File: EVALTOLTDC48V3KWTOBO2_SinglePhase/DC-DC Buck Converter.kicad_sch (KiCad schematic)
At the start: 39 parts, among them J3 EXT/ITN 12V, J4 +12V_EXT, J5 +5V_EXT, Q9 FMMT723/SOT, U1 ILD8150XUMA1

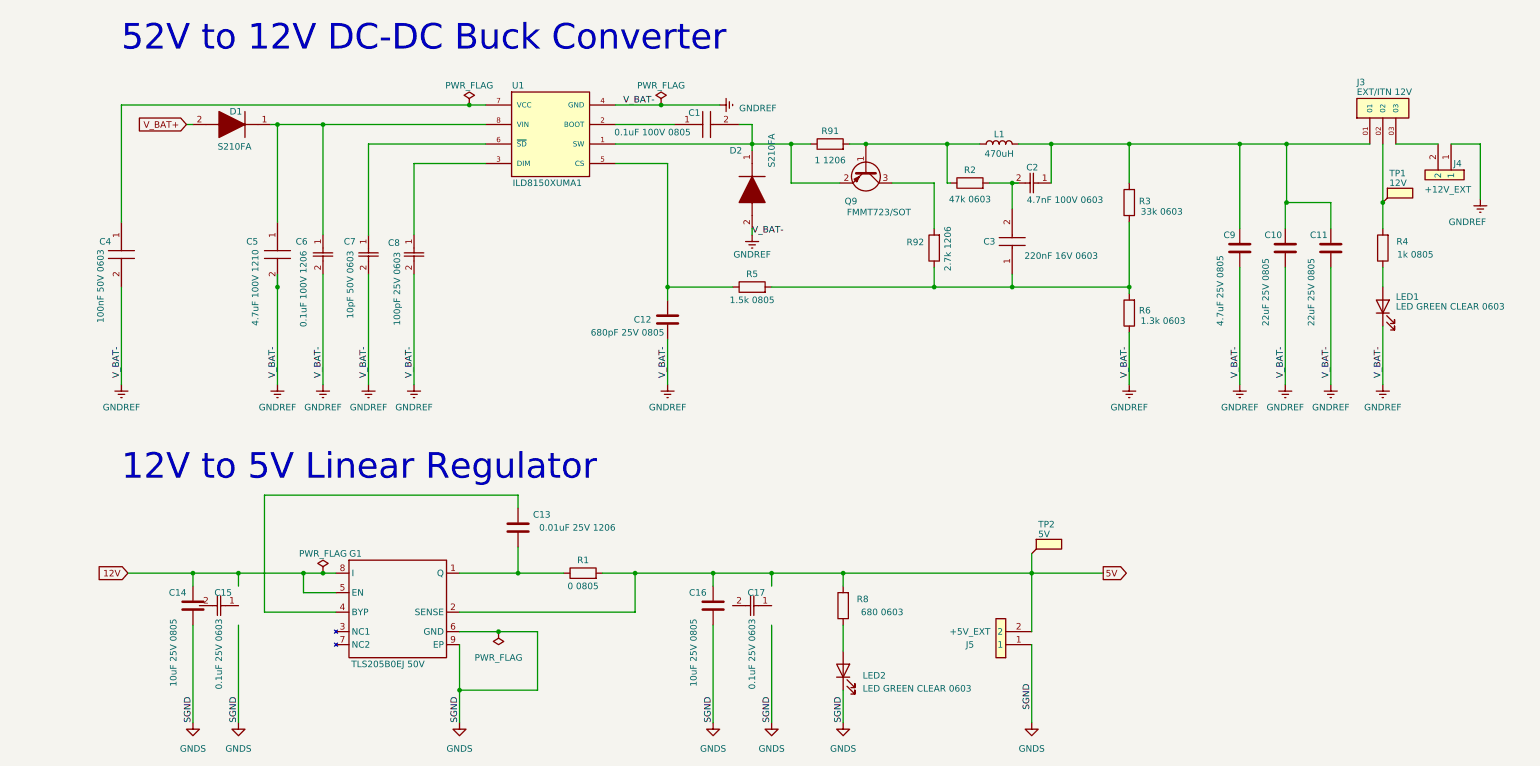
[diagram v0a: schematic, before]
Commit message: Change 1
Changed DC-DC Buck Converter and U Phase
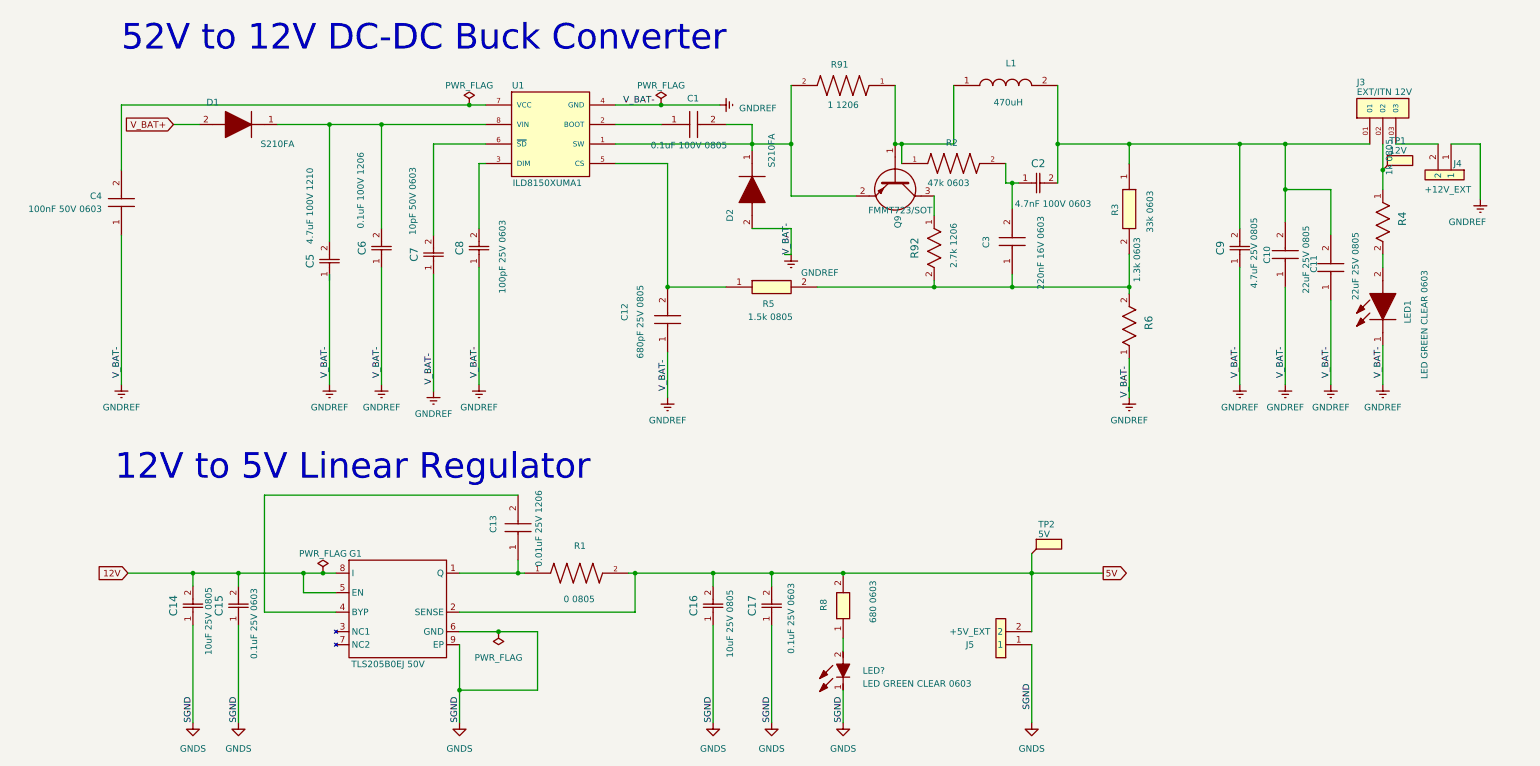
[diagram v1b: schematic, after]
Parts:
- C1: footprint just-footprints:C0805 -> C0805
- C10, C11: footprint (none) -> CAPC2012X145N; symbol Device:C -> C2012X7S1A226M125AC:C2012X7S1A226M125AC; Height (none) -> 1.45; Manufacturer_Name (none) -> TDK; Manufacturer_Part_Number (none) -> C2012X7S1A226M125AC
- C12: footprint (none) -> C1206C103J3RACAUTO:C1206; symbol Device:C -> C1206C103J3RACAUTO:C1206C103J3RACAUTO; Manufacturer_Name (none) -> KEMET; Manufacturer_Part_Number (none) -> C1206C103J3RACAUTO; Mouser Part Number (none) -> 80-C1206C103J3RAUTO; Mouser Price/Stock (none) -> https://www.mouser.co.uk/ProductDetail/KEMET/C1206C103J3RAC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
- C13: footprint (none) -> C1206; symbol Device:C -> C1206C103J3RACAUTO:C1206C103J3RACAUTO; Manufacturer_Name (none) -> KEMET; Manufacturer_Part_Number (none) -> C1206C103J3RACAUTO; Mouser Part Number (none) -> 80-C1206C103J3RAUTO; Mouser Price/Stock (none) -> https://www.mouser.co.uk/ProductDetail/KEMET/C1206C103J3RAC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
- C14, C16: footprint (none) -> CAPC220145_145N_KEM; symbol Device:C -> C0805C106M3PACTU:C0805C106M3PACTU
- C15, C17: footprint just-footprints:CAPC17795_95N_KEM -> CAPC17795_95N_KEM; symbol C0603X104M3RAUTO:C0603X104M3RACTU -> C0603X104M3RACTU:C0603X104M3RACTU
- C2: footprint just-footprints:CAPC17795_95N_KEM -> CAPC17795_95N_KEM
- C3: footprint just-footprints:C0603 -> C0603
- C4: footprint just-footprints:CAPC1608X95N -> CAPC1608X95N
- C5: footprint just-footprints:CAPC3225X280N -> CAP_CNC6_TDK; symbol CNA6P1X7R2A475K250AE:CNA6P1X7R2A475K250AE -> CNC6P1X7R2A475K250AE:CNC6P1X7R2A475K250AE; Height 2.8 -> (none); Manufacturer_Name TDK -> (none); Manufacturer_Part_Number CNA6P1X7R2A475K250AE -> (none); Mouser Part Number 810-CNA6P1X7R2A475K2 -> (none); Mouser Price/Stock https://www.mouser.co.uk/ProductDetail/TDK/CNA6P1X7R2A475K2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 -> (none)
- C6: footprint just-footprints:CAP_C1206F-RAC-ER_KEM -> CAP_C1206F-RAC-ER_KEM
- C7: footprint just-footprints:CAPC17595_87N_KEM -> CAPC17595_87N_KEM
- C8: footprint just-footprints:CAPC10555_55N_KEM -> CAPC17595_87N_KEM; symbol C0603C101K3RACAUTO:C0402C101K3RACTU -> C0603C101K3RACAUTO:C0603C101K3RACAUTO
- C9: footprint (none) -> CAPC220145_88N_KEM; symbol Device:C -> C0805X475K3RAC7800:C0805C681J5RACTU
- D1, D2: footprint just-footprints:SODFL3618X143N -> SODFL3618X143N
- G1: footprint (none) -> TLS205B0EJV50XUMA1:SOIC127P600X170-9N
- J4, J5: footprint just-footprints:1725656 -> 1725656
- L1: footprint (none) -> WE-PD_1260/1245/1280/121054; symbol Device:L -> 7447709471:7447709471; Manufacturer_Name (none) -> Wurth Elektronik; Manufacturer_Part_Number (none) -> 7447709471; Mouser Part Number (none) -> 710-7447709471; Mouser Price/Stock (none) -> https://www.mouser.co.uk/ProductDetail/Wurth-Elektronik/744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
- LED1: footprint (none) -> LEDC1608X80N; symbol Device:LED -> LTST-C190KGKT:LTST-C190KGKT; Arrow Part Number (none) -> LTST-C190KGKT; Arrow Price/Stock (none) -> https://www.arrow.com/en/products/ltst-c190kgkt/lite-on-tec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; Height (none) -> 0.8; Manufacturer_Name (none) -> Lite-On; Manufacturer_Part_Number (none) -> LTST-C190KGKT; Mouser Part Number (none) -> 859-LTST-C190KGKT; Mouser Price/Stock (none) -> https://www.mouser.co.uk/ProductDetail/Lite-On/LTST-C190KGK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
- LED?: renamed from LED2; footprint (none) -> LEDC1608X80N; symbol Device:LED -> LTST-C190KGKT:LTST-C190KGKT; Arrow Part Number (none) -> LTST-C190KGKT; Arrow Price/Stock (none) -> https://www.arrow.com/en/products/ltst-c190kgkt/lite-on-tec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; Height (none) -> 0.8; Manufacturer_Name (none) -> Lite-On; Manufacturer_Part_Number (none) -> LTST-C190KGKT; Mouser Part Number (none) -> 859-LTST-C190KGKT; Mouser Price/Stock (none) -> https://www.mouser.co.uk/ProductDetail/Lite-On/LTST-C190KGK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
- Q9: footprint Package_TO_SOT_SMD:SOT-23 -> SOT96P240X110-3N; symbol Transistor_BJT:BC858 -> FMMT723QTA:FMMT723QTA; Height (none) -> 1.1; Manufacturer_Name (none) -> Diodes Incorporated; Manufacturer_Part_Number (none) -> FMMT723QTA; Mouser Part Number (none) -> 621-FMMT723QTA; Mouser Price/Stock (none) -> https://www.mouser.co.uk/ProductDetail/Diodes-Incorporated/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
- R1: footprint (none) -> RCS08050000Z0EA:RESC2012X50N; symbol Device:R -> RCS08050000Z0EA:RCS08050000Z0EA
- R2: footprint (none) -> RCS060347K0FKEA:RESC1508X50N; symbol Device:R -> RCS060347K0FKEA:RCS060347K0FKEA
- R3: footprint (none) -> RESC1608X50N; symbol Device:R -> RCS060333K0FKEA:RCS060333K0FKEA; Height (none) -> 0.5; Manufacturer_Name (none) -> Vishay; Manufacturer_Part_Number (none) -> RCS060333K0FKEA; Mouser Part Number (none) -> 71-RCS060333K0FKEA; Mouser Price/Stock (none) -> https://www.mouser.co.uk/ProductDetail/Vishay-Dale/RCS06033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
- R4: footprint (none) -> RES_RCA0805_VIS; symbol Device:R -> RCA08051K00FKEAHP:RCA08051K00FKEAHP
- R5: footprint (none) -> RESC1608X50N; symbol Device:R -> CRCW06031R20JNEAIF:CRCW06031R20JNEAIF; Height (none) -> 0.5; Manufacturer_Name (none) -> Vishay; Manufacturer_Part_Number (none) -> CRCW06031R20JNEAIF
- R6: footprint (none) -> RC0603N_VIS; symbol Device:R -> CRCW06031K10FKTA:CRCW06031K10FKTA
- R8: footprint (none) -> RCS0603_E3; symbol Device:R -> RCS0603680RFKEA:RCS0603680RFKEA; Manufacturer_Name (none) -> Vishay; Manufacturer_Part_Number (none) -> RCS0603680RFKEA; Mouser Part Number (none) -> 71-RCS0603680RFKEA; Mouser Price/Stock (none) -> https://www.mouser.co.uk/ProductDetail/Vishay-Dale/RCS06036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
- R91: footprint (none) -> CRCW12061R00FNEB:RESC3116X60N; symbol Device:R -> CRCW12061R00FNEB:CRCW12061R00FNEB
- R92: footprint (none) -> RES_V1206_VIS; symbol Device:R -> CRCW12062K70JNEAHP:CRCW12062K70JNEAHP
- U1: footprint ILD8150XUMA1:SOIC127P600X175-8N -> ILD8150:SOIC127P600X175-8N
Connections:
- net 12V: now also C15.2
- net 5V: now also C17.2
- net GNDREF: now also C10.1, C11.1, C4.1, C6.1, C7.1, C8.1, C9.1; no longer C10.2, C11.2, C4.2, C5.2, C6.2, C7.2, C8.2, C9.2
- net GNDS: now also C15.1, C17.1
- net at U1.3 (DIM): now also C8.2; no longer C8.1
- net at C3.2, R2.2: now also C2.1; no longer C2.2
- net at C1.2, D2.1 (K), Q9.2 (E)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: now also R91.2; no longer R91.1
- net at U1.6 (~{SD}): now also C7.2; no longer C7.1
- net at U1.7 (VCC): now also C4.2; no longer C4.1
- net at D1.1 (K), U1.8 (VIN): now also C5.2, C6.2; no longer C5.1, C6.1
- net at C3.1, R5.2, R6.2: now also R3.2, R92.2; no longer R3.1, R92.1
- net at R4.1: now also J3.02, TP1.1; no longer LED1.2 (A)
- net at Q9.3 (C): now also R92.1; no longer R92.2
- net at L1.1, Q9.1 (B), R2.1: now also R91.1; no longer R91.2
- new net: C10.2, C11.2, C2.2, C9.2, J3.01, L1.2, R3.1
- new net: LED1.2 (A), R4.2
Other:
- moved on the sheet: C1, C15, C17, C2, C4, C5, C6, C7, C8, D1, TP1

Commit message: Change 3
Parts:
- gave numbers to parts that had none: 1
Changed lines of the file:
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@@
 	(text "12V to 5V Linear Regulator"
 		(exclude_from_sim no)
-		(at 16.51 110.49 0)
+		(at 14.478 106.426 0)
 		(effects
 			(font
@@
 		(on_board yes)
 		(dnp no)
-		(fields_autoplaced yes)
 		(property "Reference" "C4"
-			(at 13.97 54.6099 90)
+			(at 24.384 54.61 90)
 			(effects
 				(font
@@
 		)
 		(property "Value" "100nF 50V 0603"
-			(at 13.97 57.1499 90)
+			(at 37.338 57.912 90)
 			(effects
 				(font
@@
 		(dnp no)
 		(fields_autoplaced yes)
-		(property "Reference" "LED?"
+		(property "Reference" "LED2"
 			(at 162.56 147.3199 90)
 			(effects
@@
 			(project "EVAL_TOLT_DC48V_3KW"
 				(path "/ab32ac57-1c18-4307-8f91-d2778314d165/9ee2cd02-96d7-461b-b7fb-170453b1d10b"
-					(reference "LED?")
+					(reference "LED2")
 					(unit 1)
 				)
@@
 		(dnp no)
 		(property "Reference" "D1"
-			(at 36.83 35.56 0)
+			(at 36.576 43.942 0)
 			(effects
 				(font

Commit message: Change 3
Added More Symbols and Footprints
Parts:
- C1: footprint C0805 -> just-footprints:C0805
- C10, C11: footprint CAPC2012X145N -> just-footprints:CAPC2012X145N
- C13: footprint C1206 -> just-footprints:C1206
- C14, C16: footprint CAPC220145_145N_KEM -> just-footprints:CAPC220145_145N_KEM
- C15, C17, C2: footprint CAPC17795_95N_KEM -> just-footprints:CAPC17795_95N_KEM
- C3: footprint C0603 -> just-footprints:C0603
- C4: footprint CAPC1608X95N -> just-footprints:CAPC1608X95N
- C5: footprint CAP_CNC6_TDK -> just-footprints:CAP_CNC6_TDK
- C6: footprint CAP_C1206F-RAC-ER_KEM -> just-footprints:CAP_C1206F-RAC-ER_KEM
- C7, C8: footprint CAPC17595_87N_KEM -> just-footprints:CAPC17595_87N_KEM
- C9: footprint CAPC220145_88N_KEM -> just-footprints:CAPC220145_88N_KEM
- D1, D2: footprint SODFL3618X143N -> just-footprints:SODFL3618X143N
- J4, J5: footprint 1725656 -> just-footprints:1725656
- LED1, LED2: footprint LEDC1608X80N -> just-footprints:LEDC1608X80N
- Q9: footprint SOT96P240X110-3N -> just-footprints:SOT96P240X110-3N
- R3, R5: footprint RESC1608X50N -> just-footprints:RESC1608X50N
- R4: footprint RES_RCA0805_VIS -> just-footprints:RES_RCA0805_VIS
- R6: footprint RC0603N_VIS -> just-footprints:RC0603N_VIS
- R8: footprint RCS0603_E3 -> just-footprints:RCS0603_E3
- R92: footprint RES_V1206_VIS -> just-footprints:RES_V1206_VIS
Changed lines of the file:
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@@
 			)
 		)
-		(property "Footprint" "CAPC2012X145N"
+		(property "Footprint" "just-footprints:CAPC2012X145N"
 			(at 350.19 66.04 0)
 			(effects
@@
 			)
 		)
-		(property "Footprint" "CAPC220145_145N_KEM"
+		(property "Footprint" "just-footprints:CAPC220145_145N_KEM"
 			(at 133.35 138.43 0)
 			(effects
@@
 			)
 		)
-		(property "Footprint" "CAPC220145_88N_KEM"
+		(property "Footprint" "just-footprints:CAPC220145_88N_KEM"
 			(at 236.22 68.58 0)
 			(effects
@@
 			)
 		)
-		(property "Footprint" "CAPC17595_87N_KEM"
+		(property "Footprint" "just-footprints:CAPC17595_87N_KEM"
 			(at 87.63 68.58 0)
 			(effects
@@
 			)
 		)
-		(property "Footprint" "CAPC17795_95N_KEM"
+		(property "Footprint" "just-footprints:CAPC17795_95N_KEM"
 			(at 193.04 52.07 0)
 			(effects
@@
 			)
 		)
-		(property "Footprint" "C0805"
+		(property "Footprint" "just-footprints:C0805"
 			(at 132.08 136.83 0)
 			(effects
@@
 			)
 		)
-		(property "Footprint" "CAPC17795_95N_KEM"
+		(property "Footprint" "just-footprints:CAPC17795_95N_KEM"
 			(at 40.64 138.43 0)
 			(effects
@@
 			)
 		)
-		(property "Footprint" "CAP_CNC6_TDK"
+		(property "Footprint" "just-footprints:CAP_CNC6_TDK"
 			(at 58.42 71.12 0)
 			(effects
@@
 			)
 		)
-		(property "Footprint" "RESC1608X50N"
+		(property "Footprint" "just-footprints:RESC1608X50N"
 			(at 149.86 168.58 0)
 			(effects
@@
 			)
 		)
-		(property "Footprint" "RES_RCA0805_VIS"
+		(property "Footprint" "just-footprints:RES_RCA0805_VIS"
 			(at 264.16 53.34 0)
 			(effects
@@
 			)
 		)
-		(property "Footprint" "RES_V1206_VIS"
+		(property "Footprint" "just-footprints:RES_V1206_VIS"
 			(at 176.53 58.42 0)
 			(effects
@@
 			)
 		)
-		(property "Footprint" "SOT96P240X110-3N"
+		(property "Footprint" "just-footprints:SOT96P240X110-3N"
 			(at 67.64 58.42 0)
 			(effects
@@
 			)
 		)
-		(property "Footprint" "CAPC1608X95N"
+		(property "Footprint" "just-footprints:CAPC1608X95N"
 			(at 113.97 53.34 0)
 			(effects
@@
 			)
 		)
-		(property "Footprint" "1725656"
+		(property "Footprint" "just-footprints:1725656"
 			(at 212.09 237.16 0)
 			(effects
@@
 			)
 		)
-		(property "Footprint" "1725656"
+		(property "Footprint" "just-footprints:1725656"
 			(at 372.415 27.94 0)
 			(effects
@@
 			)
 		)
-		(property "Footprint" "LEDC1608X80N"
+		(property "Footprint" "just-footprints:LEDC1608X80N"
 			(at 252.4 143.51 0)
 			(effects
@@
 			)
 		)
-		(property "Footprint" "RC0603N_VIS"
+		(property "Footprint" "just-footprints:RC0603N_VIS"
 			(at 214.63 73.66 0)
 			(effects
@@
 			)
 		)
-		(property "Footprint" "C1206"
+		(property "Footprint" "just-footprints:C1206"
 			(at 191.44 116.84 0)
 			(effects
@@
 			)
 		)
-		(property "Footprint" "LEDC1608X80N"
+		(property "Footprint" "just-footprints:LEDC1608X80N"
 			(at 357.81 71.12 0)
 			(effects
@@
 			)
 		)
-		(property "Footprint" "SODFL3618X143N"
+		(property "Footprint" "just-footprints:SODFL3618X143N"
 			(at 238.43 57.15 0)
 			(effects
@@
 			)
 		)
-		(property "Footprint" "CAPC2012X145N"
+		(property "Footprint" "just-footprints:CAPC2012X145N"
 			(at 341.3 63.5 0)
 			(effects
@@
 			)
 		)
-		(property "Footprint" "CAPC17595_87N_KEM"
+		(property "Footprint" "just-footprints:CAPC17595_87N_KEM"
 			(at 78.74 69.85 0)
 			(effects
@@
 			)
 		)
-		(property "Footprint" "SODFL3618X143N"
+		(property "Footprint" "just-footprints:SODFL3618X143N"
 			(at 36.83 138.1 0)
 			(effects
@@
 			)
 		)
-		(property "Footprint" "RCS0603_E3"
+		(property "Footprint" "just-footprints:RCS0603_E3"
 			(at 254.94 129.54 0)
 			(effects
@@
 			)
 		)
-		(property "Footprint" "C0603"
+		(property "Footprint" "just-footprints:C0603"
 			(at 287.96 60.96 0)
 			(effects
@@
 			)
 		)
-		(property "Footprint" "CAPC220145_145N_KEM"
+		(property "Footprint" "just-footprints:CAPC220145_145N_KEM"
 			(at 31.75 138.43 0)
 			(effects
@@
 			)
 		)
-		(property "Footprint" "CAPC17795_95N_KEM"
+		(property "Footprint" "just-footprints:CAPC17795_95N_KEM"
 			(at 144.78 138.43 0)
 			(effects
@@
 			)
 		)
-		(property "Footprint" "CAP_C1206F-RAC-ER_KEM"
+		(property "Footprint" "just-footprints:CAP_C1206F-RAC-ER_KEM"
 			(at 68.58 68.58 0)
 			(effects
@@
 			)
 		)
-		(property "Footprint" "RESC1608X50N"
+		(property "Footprint" "just-footprints:RESC1608X50N"
 			(at 118.44 62.23 0)
 			(effects
